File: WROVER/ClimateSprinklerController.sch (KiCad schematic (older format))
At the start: 189 parts, among them J1 7.5 TO 40 V, J10 DISPLAY_2, J11 HVAC, J12 RELAY, J2 POWER SEL, J3 EXT_ENC, J4 SERIAL, J5 SPI, J6 I2C, J7 PIR, J8 IO_EXP, J9 DISPLAY_1, K1 G5Q-1-DC5, K2 G5Q-1-DC5, K3 G5Q-1-DC5, Q1 TEPT5700, Q10 2N6073B, Q11 2N6073B, Q12 2N6073B, Q2 2N7002, Q3 2N7002, Q4 2N7002, Q5 2N6073B, Q6 2N6073B, Q7 2N6073B, Q8 2N6073B, Q9 2N6073B, SW1 RESET, SW2 MODE, SW3 PEC11S-929K-S0015, U1 ESP32-WROVER, U10 MOC3043, U11 MOC3043, U12 MOC3043, U13 MOC3043, U14 MOC3043, U15 MOC3043, U16 MOC3043, U17 MOC3043, U2 MCP23017_SO, U3 LMR36520, U4 LD1086DT33TR, U5 SGP40-Sensor_Air_Quality, U6 TMP117, U7 DHT22, U8 BME280, U9 SHTC3

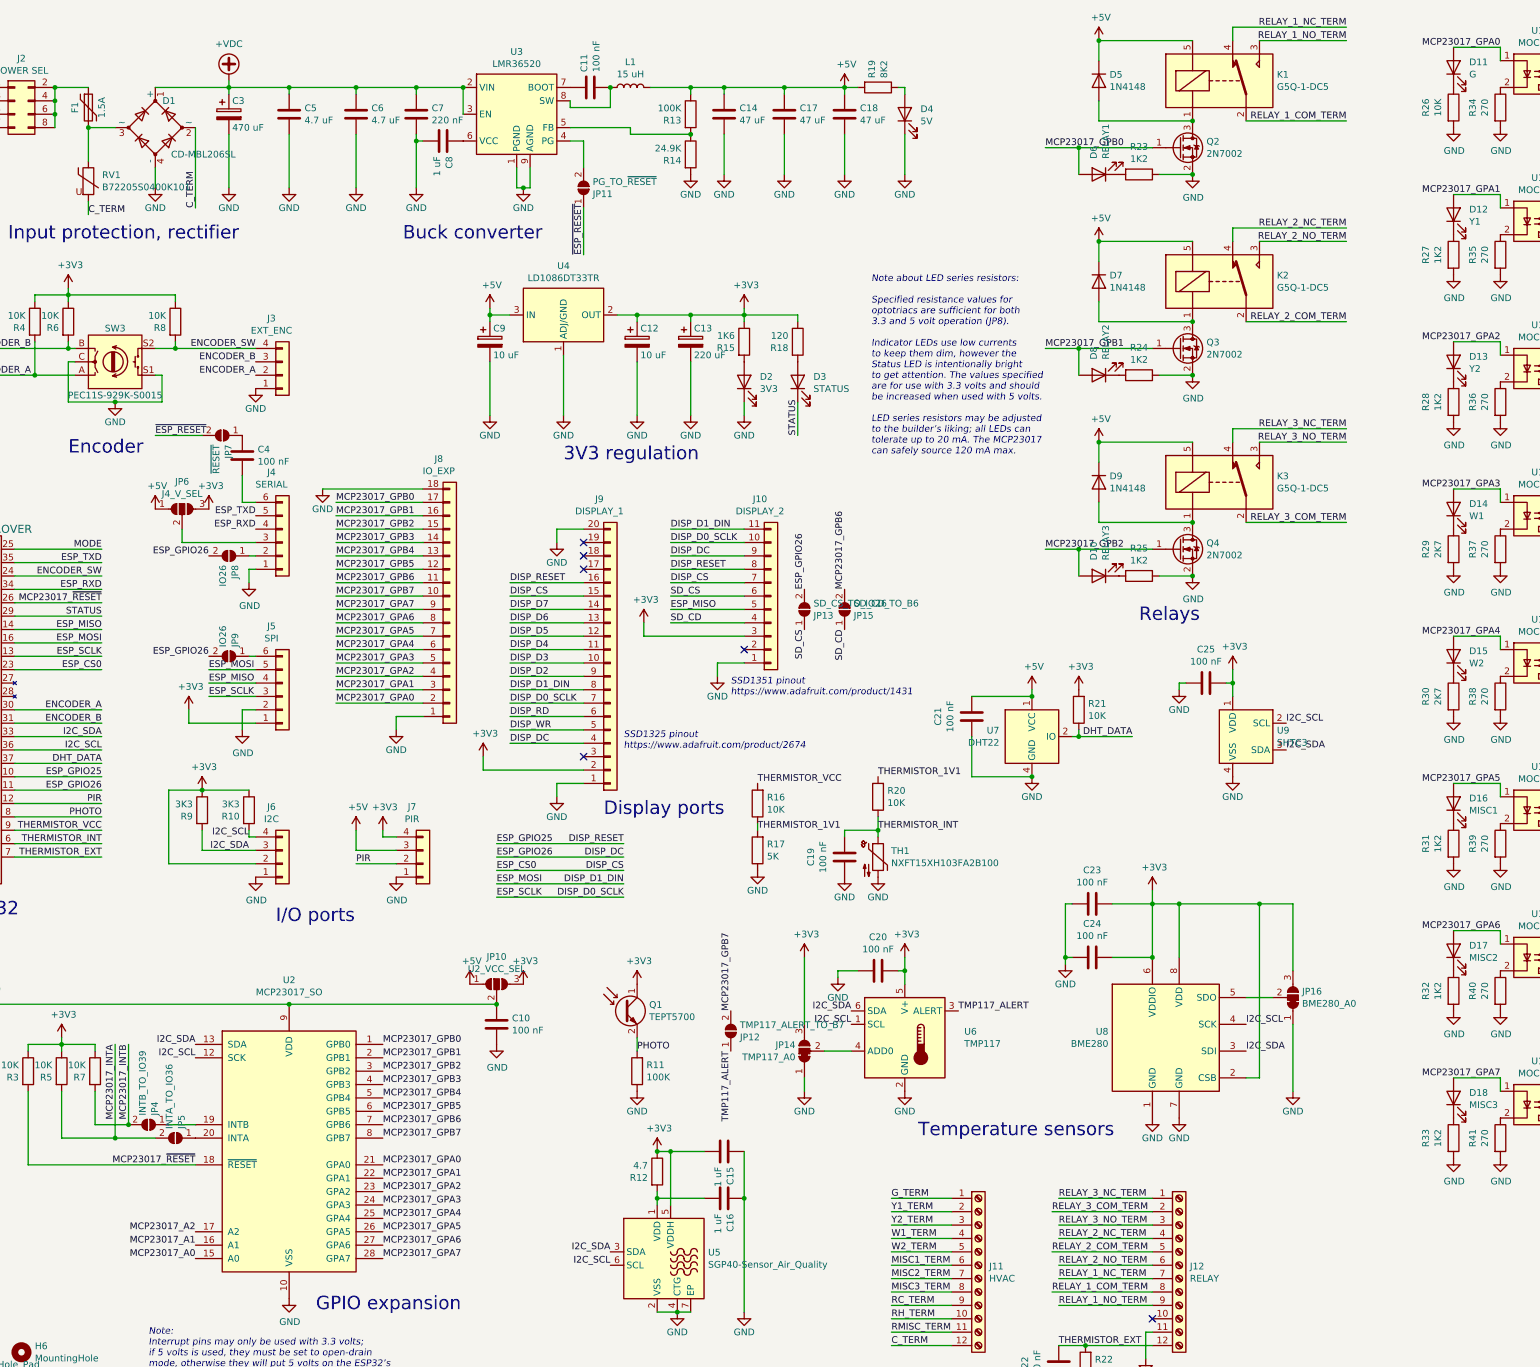
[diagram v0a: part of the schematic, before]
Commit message: Doc updates, new images, new enclosures, regenerate gerbers
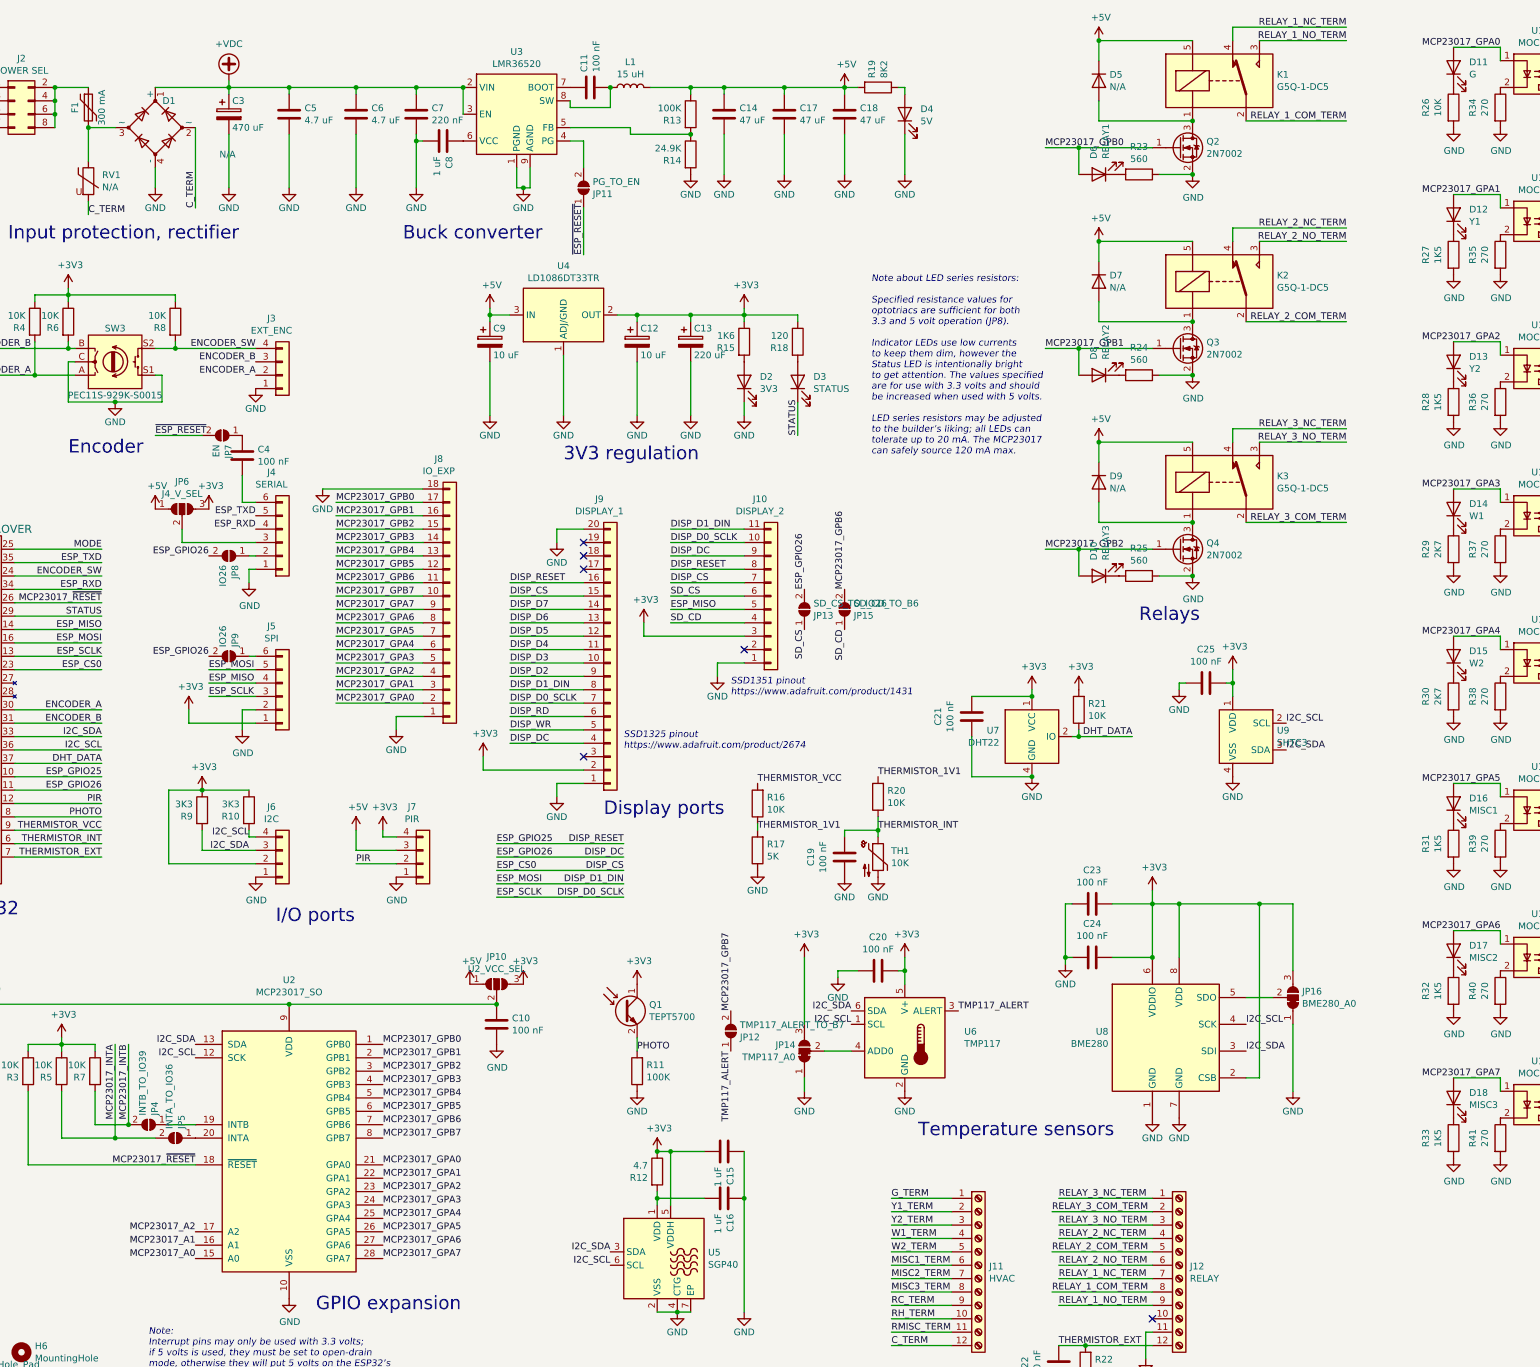
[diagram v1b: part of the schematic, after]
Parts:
- C1: MPN1 (none) -> C2012X5R1V106K085AC; Part C2012X5R1V106K085AC -> (none)
- C10, C11, C19, C2, C20, C21, C22, C23, C24, C25, C4: MPN1 (none) -> CC0805KRX7R7BB104; Part CC0805KRX7R7BB104 -> (none)
- C12, C9: MPN1 (none) -> EEE-HP0J100R; Part EEE-HP0J100R -> (none)
- C13: MPN1 (none) -> EEE-HB0J221AP; Part EEE-HB0J221AP -> (none)
- C14, C17, C18: MPN1 (none) -> GRM32ER61C476KE15L; Part GRM32ER61C476KE15L -> (none)
- C15, C16, C8: MPN1 (none) -> C0805C105K4RACTU; Part C0805C105K4RACTU -> (none)
- C26, C27, C28, C29, C30, C31, C32, C33: MPN1 (none) -> CC0805KRX7R9BB103; Part CC0805KRX7R9BB103 -> (none)
- C3: MPN1 (none) -> EEV-FK1H471M; Part EEV-FK1H471M -> (none)
- C5, C6: MPN1 (none) -> C2012X5R1H475K125AB; Part C2012X5R1H475K125AB -> (none)
- C7: MPN1 (none) -> C2012X5R1H224K125AA; Part C2012X5R1H224K125AA -> (none)
- D1: value CD-MBL206SL -> N/A; MPN1 (none) -> CD-MBL206SL; Part CD-MBL206SL -> (none)
- D10, D6, D8: MPN1 (none) -> APTL3216CGCK; Part APTL3216CGCK -> (none)
- D11: MPN1 (none) -> APTL3216ZGC; Part APTL3216ZGC -> (none)
- D12, D13: MPN1 (none) -> APTL3216QBC/D; Part APTL3216QBC/D -> (none)
- D14, D15: MPN1 (none) -> APTL3216SURCK; Part APTL3216SURCK -> (none)
- D16, D17, D18: MPN1 (none) -> APTL3216SYCK; Part APTL3216SYCK -> (none)
- D2, D4: MPN1 (none) -> 597-6901-607F; Part 597-6901-607F -> (none)
- D3: MPN1 (none) -> APTL3216SECK; Part APTL3216SECK -> (none)
- D5, D7, D9: value 1N4148 -> N/A; MPN1 (none) -> 1N4148W; Part 1N4148W -> (none)
- F1: value 1.5A -> 300 mA; MPN1 (none) -> 2920L030DR; Part 2920L150DR -> (none)
- H1, H2, H3, H4, H5, H6, J10, J2, J3, J4, J5, J6, J7, J8, J9, JP1, JP10, JP12, JP13, JP14, JP15, JP16, JP2, JP3, JP4, JP5, JP6, JP8, JP9: MPN1 (none) -> N/A; Population (none) -> DNF
- J1: MPN1 (none) -> 694106301002; Part 694106301002 -> (none)
- J11, J12: MPN1 (none) -> 1862039
- JP11: value PG_TO_~RESET -> PG_TO_EN; MPN1 (none) -> N/A; Population (none) -> DNF
- JP7: value ~RESET -> EN; MPN1 (none) -> N/A; Population (none) -> DNF
- K1, K2, K3: MPN1 (none) -> G5Q-1-DC5; Part G5Q-1-DC5 -> (none)
- L1: MPN1 (none) -> 7447709150; MPN2 (none) -> MSS1210-153MEB; Part 7447709150 -> (none); PartAlt MSS1210-153MEB -> (none)
- Q1: MPN1 (none) -> TEPT5700; Part TEPT5700 -> (none)
- Q10, Q11, Q12, Q5, Q6, Q7, Q8, Q9: MPN1 (none) -> 2N6073BG; Part 2N6073BG -> (none)
- Q2, Q3, Q4: MPN1 (none) -> 2N7002; Part 2N7002 -> (none)
- R1, R16, R2, R20, R21, R22, R3, R4, R5, R6, R7, R8: MPN1 (none) -> RC0805FR-0710KL; Part RC0805FR-0710KL -> (none)
- R10, R9: MPN1 (none) -> RT0805FRE073K3L; Part RT0805FRE073K3L -> (none)
- R11, R12, R13: MPN1 (none) -> RC0805FR-07100KL; Part RC0805FR-07100KL -> (none)
- R14: MPN1 (none) -> RT0805FRE0724K9L; Part RT0805FRE0724K9L -> (none)
- R15: MPN1 (none) -> RT0805FRE071K6L; Part RT0805FRE071K6L -> (none)
- R17: MPN1 (none) -> CRCW08055K00JNTA; Part CRCW08055K00JNTA -> (none)
- R18: MPN1 (none) -> RT0805FRE07120RL; Part RT0805FRE07120RL -> (none)
- R19: MPN1 (none) -> RT0805FRE078K2L; Part RT0805FRE078K2L -> (none)
- R23, R24, R25: value 1K2 -> 560; MPN1 (none) -> RT0805FRE07560RL; Part RT0805FRE071K2L -> (none)
- R26: MPN1 (none) -> RC0805FR-0710KL; Part RT0805FRE079K1L -> (none)
- R27, R28, R31, R32, R33: value 1K2 -> 1K5; MPN1 (none) -> RT0805FRE071K5L; Part RT0805FRE072K7L -> (none)
- R29, R30: MPN1 (none) -> RT0805FRE072K7L; Part RT0805FRE072K7L -> (none)
- R34, R35, R36, R37, R38, R39, R40, R41: MPN1 (none) -> RT0805FRE07270RL; Part RT0805FRE07270RL -> (none)
- R42, R43, R44, R45, R46, R47, R48, R49: MPN1 (none) -> RT0805FRE07180RL; Part RT0805FRE07180RL -> (none)
- R50, R51, R52, R53, R54, R55, R56, R57: MPN1 (none) -> RT0805FRE07820RL; Part RT0805FRE07820RL -> (none)
- R58, R59, R60, R61, R62, R63, R64, R65: MPN1 (none) -> ERJ-P06J390V; Part ERJ-P06J390V -> (none)
- RV1: value B72205S0400K101 -> N/A; MPN1 (none) -> B72205S0400K101; Part B72205S0400K101 -> (none)
- SW1, SW2: MPN1 (none) -> PTS645VK582LFS; Part PTS645VK582LFS -> (none)
- SW3: MPN1 (none) -> PEC11S-929K-S0015; Part PEC11S-929K-S0015 -> (none)
- TH1: value NXFT15XH103FA2B100 -> 10K; MPN1 (none) -> NXFT15XH103FA2B100; Part NXFT15XH103FA2B100 -> (none)
- U1: MPN1 (none) -> ESP32-WROVER
- U10, U11, U12, U13, U14, U15, U16, U17: MPN1 (none) -> MOC3043SM; Part MOC3043SM -> (none)
- U2: MPN1 (none) -> MCP23017-E/SO; Part MCP23017-E/SO -> (none)
- U3: MPN1 (none) -> LMR36520ADDAR; Part LMR36520ADDAR -> (none)
- U4: MPN1 (none) -> LD1086DT33TR; Part LD1086DT33TR -> (none)
- U5: value SGP40-Sensor_Air_Quality -> SGP40; MPN1 (none) -> SGP40
- U6: MPN1 (none) -> TMP117MAIDRVR; Part TMP117MAIDRVR -> (none)
- U7: MPN1 (none) -> DHT22; Part DHT22 -> (none)
- U8: MPN1 (none) -> BME280; Part BME280 -> (none)
- U9: MPN1 (none) -> SHTC3; Part SHTC3 -> (none)
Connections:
- net +3V3: now also C21.1, U7.1 (VCC)
- net +5V: no longer C21.1, U7.1 (VCC)
